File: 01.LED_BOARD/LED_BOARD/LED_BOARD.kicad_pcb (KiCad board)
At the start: 2 copper layers, 4 parts, among them SW1 SW_DPDT_x2

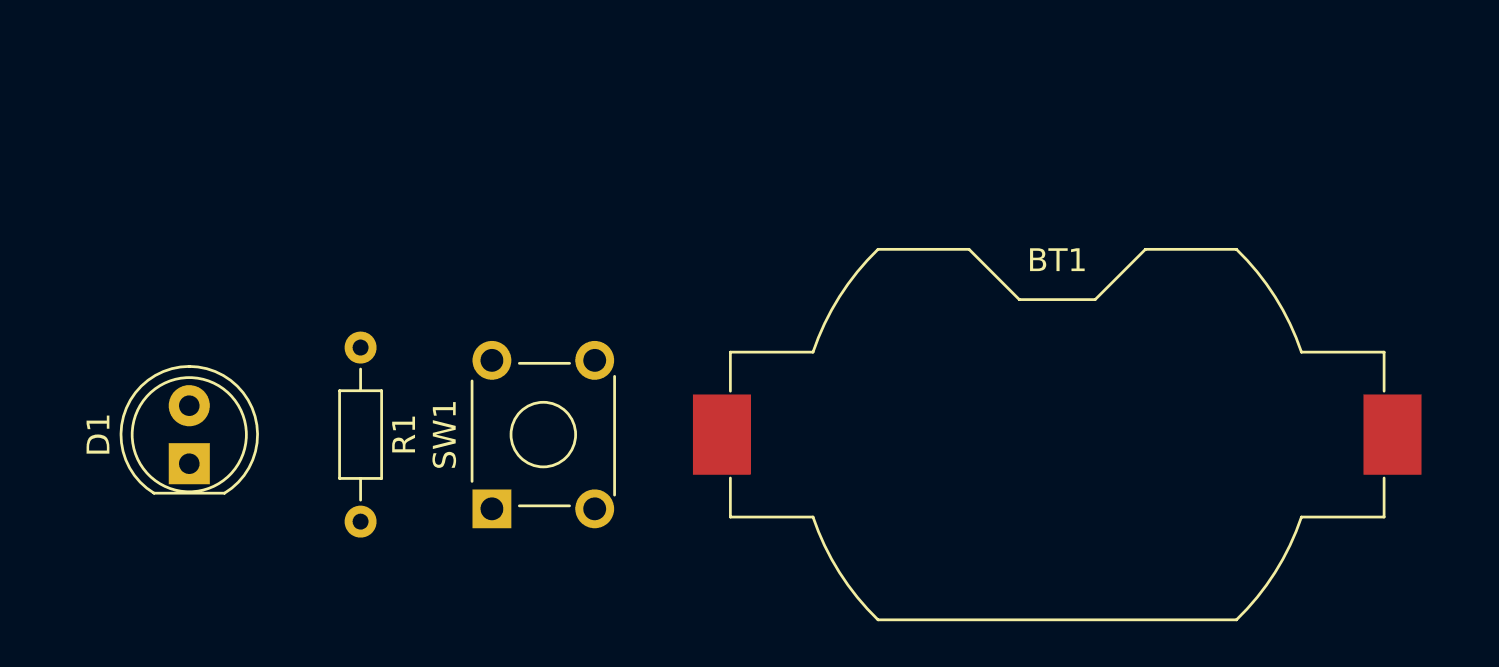
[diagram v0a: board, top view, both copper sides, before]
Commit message: LED BOARD - PCB - OUTLINE AND CONSTRAINTS
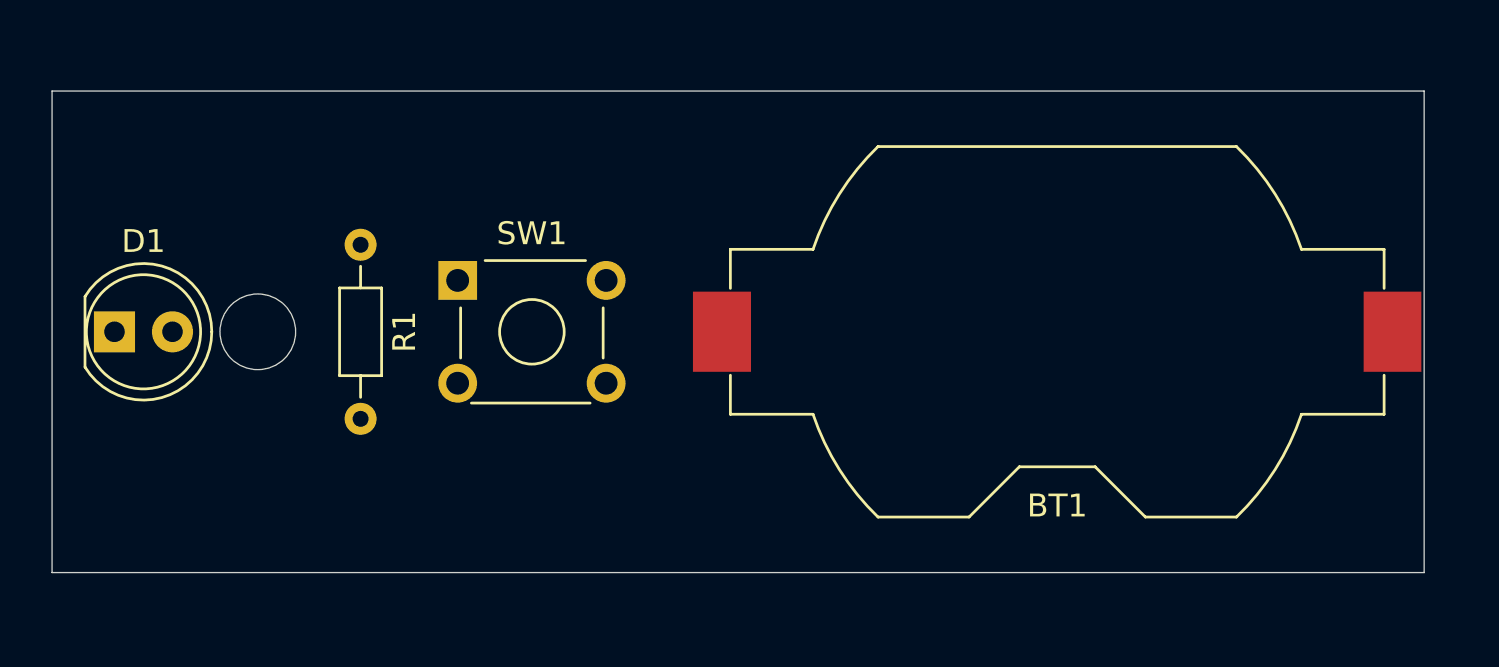
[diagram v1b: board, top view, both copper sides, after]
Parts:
- moved SW1 10.1 mm to (144.2, 90.8), turned to 0 degrees
- moved D1 6.64 mm to (129.2, 93.0), turned to 0 degrees
- moved BT1 4.50 mm to (170.5, 93.0), turned to 0 degrees
- moved R1 4.50 mm to (140.0, 89.2)
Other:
- board outline added: 60.1 x 21.1 mm

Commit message: LED BOARD - PCB - ROUTE
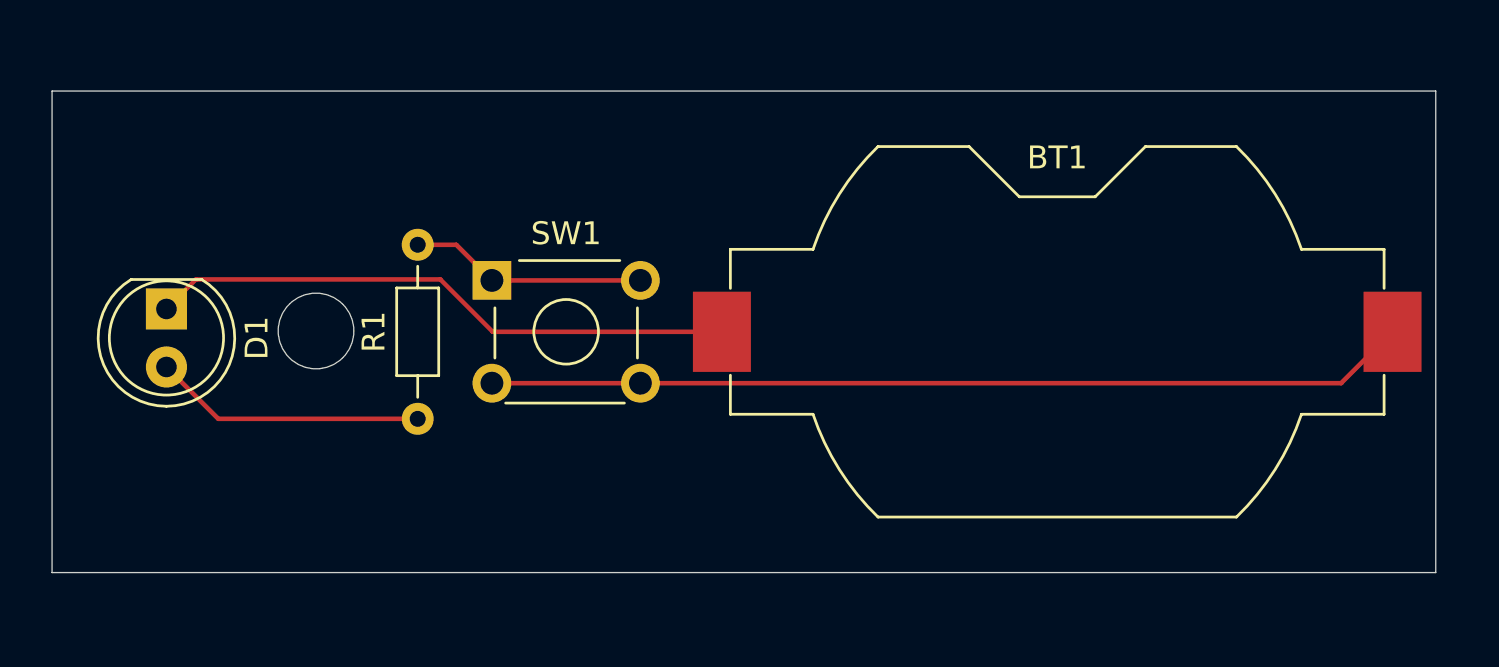
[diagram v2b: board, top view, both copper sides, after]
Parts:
- moved R1 8.02 mm to (142.5, 96.8), turned to 90 degrees
- moved D1 2.49 mm to (131.5, 92.0), turned to -90 degrees
- moved SW1 1.50 mm to (145.8, 90.8)
- turned BT1 to 180 degrees
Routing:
- net /BAT_POS: track 0.00 -> 40.4 mm
- net /LED_CATHODE: track 0.00 -> 25.8 mm
- net /LED_ANODE: track 0.00 -> 11.9 mm
- net Net-(SW1A-A): track 0.00 -> 10.4 mm
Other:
- board size 60.1 x 21.1 mm -> 60.6 x 21.1 mm

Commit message: LEDBOARD - PCB - REFINED OUTLINE AND CONSTRAINTS
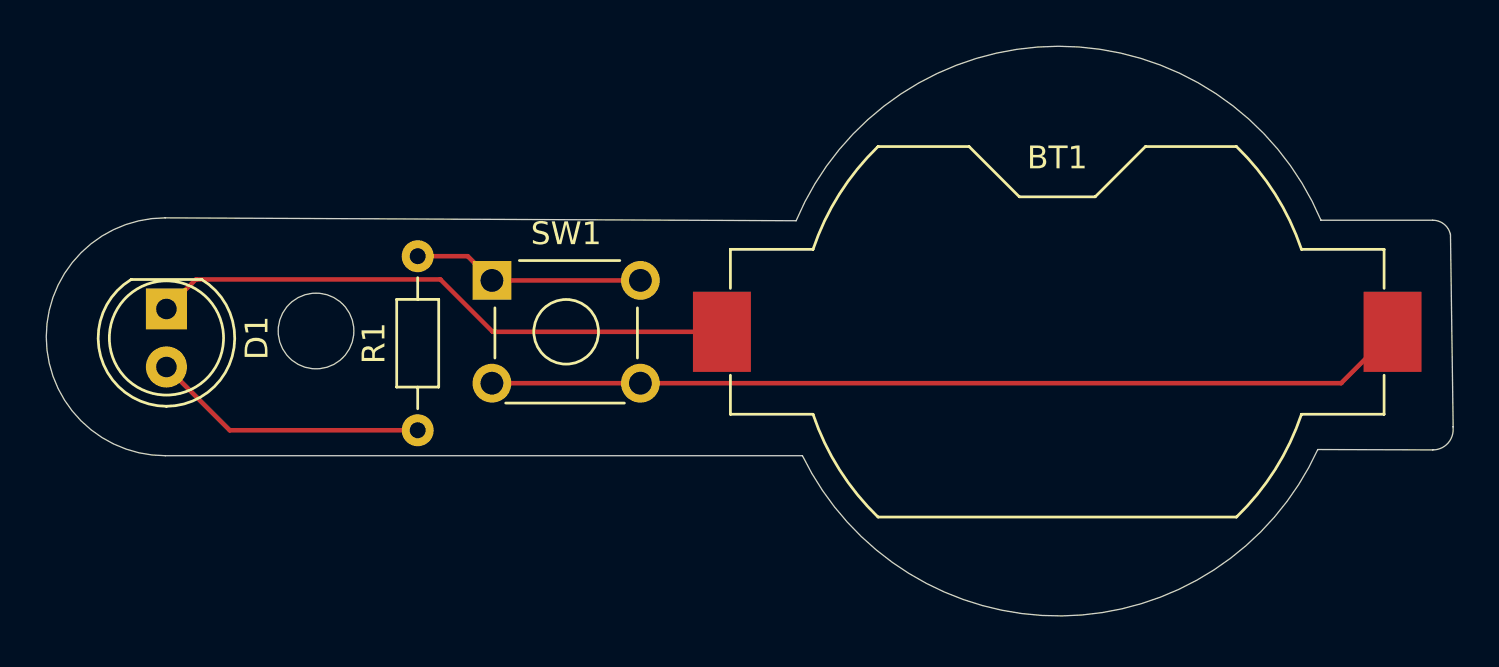
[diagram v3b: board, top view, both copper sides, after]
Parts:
- moved R1 0.50 mm to (142.5, 97.3)
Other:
- board size 60.6 x 21.1 mm -> 61.6 x 24.9 mm
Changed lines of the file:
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@@
 	(footprint "Resistor_THT:R_Axial_DIN0204_L3.6mm_D1.6mm_P7.62mm_Horizontal"
 		(layer "F.Cu")
-		(at 142.5 96.81 90)
+		(at 142.5 97.31 90)
 		(descr "Resistor, Axial_DIN0204 series, Axial, Horizontal, pin pitch=7.62mm, 0.167W, length*diameter=3.6*1.6mm^2, http://cdn-reichelt.de/documents/datenblatt/B400/1_4W%23YAG.pdf")
 		(tags "Resistor Axial_DIN0204 series Axial Horizontal pin pitch 7.62mm 0.167W length 3.6mm diameter 1.6mm")
@@
 		)
 	)
-	(gr_rect
-		(start 126.492 82.459)
-		(end 187.071 103.541)
-		(stroke
-			(width 0.05)
-			(type default)
-		)
-		(fill no)
+	(gr_line
+		(start 182.044915 88.115236)
+		(end 186.934616 88.115232)
+		(stroke
+			(width 0.05)
+			(type default)
+		)
+		(layer "Edge.Cuts")
+	)
+	(gr_line
+		(start 131.445 88.011)
+		(end 159.0675 88.138)
+		(stroke
+			(width 0.05)
+			(type default)
+		)
+		(layer "Edge.Cuts")
+	)
+	(gr_arc
+		(start 131.445 98.425)
+		(mid 126.238 93.218)
+		(end 131.445 88.011)
+		(stroke
+			(width 0.05)
+			(type default)
+		)
+		(layer "Edge.Cuts")
+	)
+	(gr_arc
+		(start 186.934616 88.115232)
+		(mid 187.433744 88.28673)
+		(end 187.711403 88.735557)
+		(stroke
+			(width 0.05)
+			(type default)
+		)
 		(layer "Edge.Cuts")
 	)
@@
 		(layer "Edge.Cuts")
 	)
+	(gr_line
+		(start 187.715218 88.734739)
+		(end 187.833 97.155)
+		(stroke
+			(width 0.05)
+			(type default)
+		)
+		(layer "Edge.Cuts")
+	)
+	(gr_line
+		(start 181.906089 98.153772)
+		(end 186.944 98.171)
+		(stroke
+			(width 0.05)
+			(type default)
+		)
+		(layer "Edge.Cuts")
+	)
+	(gr_arc
+		(start 187.824065 97.156276)
+		(mid 187.615599 97.864474)
+		(end 186.944 98.171)
+		(stroke
+			(width 0.05)
+			(type default)
+		)
+		(layer "Edge.Cuts")
+	)
+	(gr_arc
+		(start 181.906089 98.153775)
+		(mid 170.710963 105.438868)
+		(end 159.343946 98.425)
+		(stroke
+			(width 0.05)
+			(type default)
+		)
+		(layer "Edge.Cuts")
+	)
+	(gr_arc
+		(start 159.0675 88.138)
+		(mid 170.54865 80.498421)
+		(end 182.044915 88.115236)
+		(stroke
+			(width 0.05)
+			(type default)
+		)
+		(layer "Edge.Cuts")
+	)
+	(gr_line
+		(start 131.445 98.425)
+		(end 159.343946 98.425)
+		(stroke
+			(width 0.05)
+			(type default)
+		)
+		(layer "Edge.Cuts")
+	)
 	(segment
 		(start 143.491063 90.706937)
@@
 	)
 	(segment
-		(start 133.77 96.81)
-		(end 142.5 96.81)
+		(start 131.5 94.54)
+		(end 134.27 97.31)
 		(width 0.2)
 		(layer "F.Cu")
@@
 	)
 	(segment
-		(start 131.5 94.54)
-		(end 133.77 96.81)
+		(start 134.27 97.31)
+		(end 142.5 97.31)
 		(width 0.2)
 		(layer "F.Cu")
 		(net 3)
+	)
+	(segment
+		(start 144.69 89.69)
+		(end 145.75 90.75)
+		(width 0.2)
+		(layer "F.Cu")
+		(net 4)
+	)
+	(segment
+		(start 142.5 89.69)
+		(end 144.69 89.69)
+		(width 0.2)
+		(layer "F.Cu")
+		(net 4)
 	)
 	(segment
@@
 		(width 0.2)
 		(layer "F.Cu")
-		(net 4)
-	)
-	(segment
-		(start 142.5 89.19)
-		(end 144.19 89.19)
-		(width 0.2)
-		(layer "F.Cu")
-		(net 4)
-	)
-	(segment
-		(start 144.19 89.19)
-		(end 145.75 90.75)
-		(width 0.2)
-		(layer "F.Cu")

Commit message: LEDBOARD - PCB - SILKSCREEN
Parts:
- BT1: value Battery_Cell -> Batt 6023
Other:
- board text added: "+"
- board text added: "-"
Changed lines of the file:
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@@
 			)
 		)
-		(property "Value" "Battery_Cell"
-			(at 0 -9.398 0)
-			(layer "F.Fab")
+		(property "Value" "Batt 6023"
+			(at 0 -11 0)
+			(layer "F.SilkS")
 			(effects
 				(font
@@
 		(property "Value" "SW_DPDT_x2"
 			(at 3.2 6.5 0)
-			(layer "F.Fab")
+			(layer "F.SilkS")
 			(effects
 				(font
@@
 		(tags "LED")
 		(property "Reference" "D1"
-			(at 1.27 -3.96 90)
+			(at -2.5 -2.5 180)
 			(layer "F.SilkS")
 			(effects
@@
 		(layer "Edge.Cuts")
 	)
+	(gr_text "-"
+		(at 154.5 91 0)
+		(layer "F.SilkS")
+		(effects
+			(font
+				(size 1 1)
+				(thickness 0.1)
+			)
+			(justify left bottom)
+		)
+	)
+	(gr_text "-"
+		(at 131 90 0)
+		(layer "F.SilkS")
+		(effects
+			(font
+				(size 1 1)
+				(thickness 0.1)
+			)
+			(justify left bottom)
+		)
+	)
+	(gr_text "+"
+		(at 131 97.5 0)
+		(layer "F.SilkS")
+		(effects
+			(font
+				(size 1 1)
+				(thickness 0.1)
+			)
+			(justify left bottom)
+		)
+	)
+	(gr_text "+"
+		(at 184.81 91.1 0)
+		(layer "F.SilkS")
+		(effects
+			(font
+				(size 1 1)
+				(thickness 0.1)
+			)
+			(justify left bottom)
+		)
+	)
 	(segment

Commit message: LED BOARD - PCB - SILKSCREEN
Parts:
- added REF**: KiCad-Logo2_6mm_SilkScreen, Symbol:KiCad-Logo2_6mm_SilkScreen, B.Cu at (170.0, 94.5)
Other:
- board text added: "Gobal Krishnan V Practice 0.0.1"

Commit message: LED BOARD
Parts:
- SW1: value SW_DPDT_x2 -> SW_DPST_x2
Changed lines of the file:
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@@
 			)
 		)
-		(property "Value" "SW_DPDT_x2"
+		(property "Value" "SW_DPST_x2"
 			(at 3.2 6.5 0)
 			(layer "F.SilkS")
